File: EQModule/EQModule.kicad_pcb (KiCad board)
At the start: 2 copper layers, 30 x 38 mm, 13 parts, among them J1 SigIn, J2 SigOut, J3 TreblePot, J4 BassPot, J5 MidPot, J6 VolPot

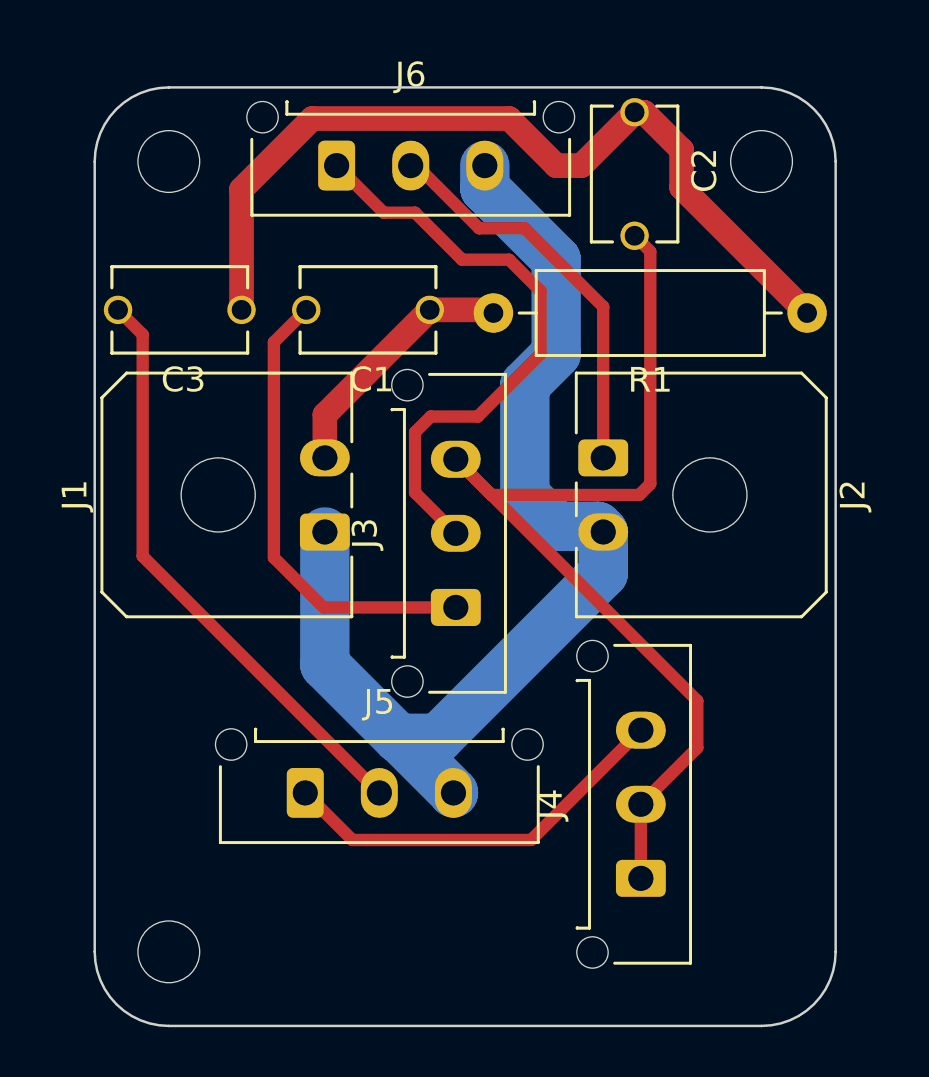
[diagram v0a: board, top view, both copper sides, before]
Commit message: Change connector footprints to contain 3D models. Make necessary PCB modifications to address errors found in the design
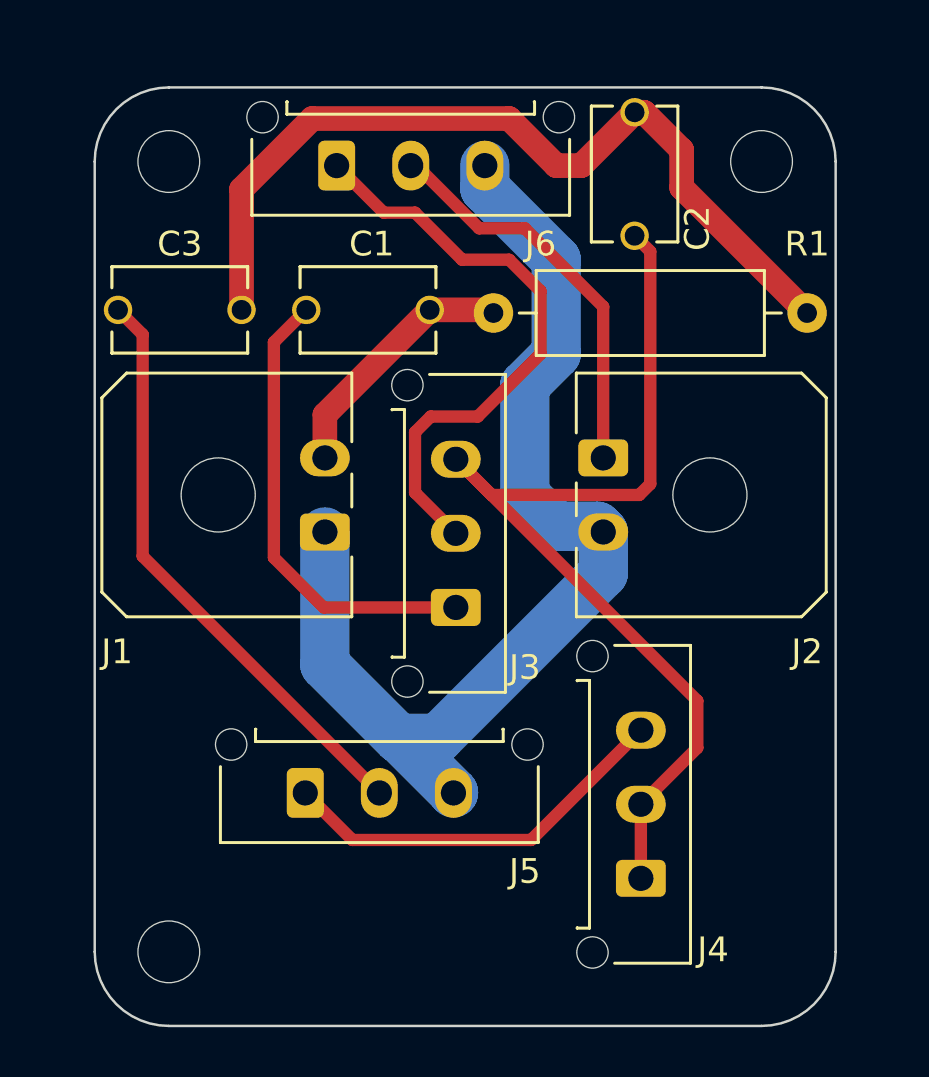
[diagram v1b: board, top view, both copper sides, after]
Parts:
- J1, J2: footprint Connector_Molex:Molex_Micro-Fit_3.0_43650-0200_1x02_P3.00mm_Horizontal -> CustomFootprints:Molex_Micro-Fit_3.0_43650-0200_1x02_P3.00mm_Horizontal
- J3, J4, J5, J6: footprint Connector_Molex:Molex_Micro-Fit_3.0_43650-0315_1x03_P3.00mm_Vertical -> CustomFootprints:Molex_Micro-Fit_3.0_43650-0315_1x03_P3.00mm_Vertical
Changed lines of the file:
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@@
   (net 8 "Net-(J3-Pin_2)")
   (net 9 "Net-(J4-Pin_3)")
-  (footprint "Connector_Molex:Molex_Micro-Fit_3.0_43650-0200_1x02_P3.00mm_Horizontal" (layer "F.Cu")
+  (footprint "CustomFootprints:Molex_Micro-Fit_3.0_43650-0200_1x02_P3.00mm_Horizontal" (layer "F.Cu")
     (at 148.59 62 -90)
     (descr "Molex Micro-Fit 3.0 Connector System, 43650-0200 (compatible alternatives: 43650-0201, 43650-0202), 2 Pins per row (https://www.molex.com/pdm_docs/sd/436500300_sd.pdf), generated with kicad-footprint-generator")
@@
     (property "ki_keywords" "screw terminal")
     (attr through_hole)
-    (fp_text reference "J2" (at 1.5 -10.12 90) (layer "F.SilkS")
-        (effects (font (size 1 1) (thickness 0.15)))
-    )
-    (fp_text value "SigOut" (at 1.5 -6.985 90) (layer "F.Fab")
-        (effects (font (size 1 1) (thickness 0.15)))
-    )
-    (fp_text user "${REFERENCE}" (at 1.5 -8.22 90) (layer "F.Fab")
+    (fp_text reference "J2" (at 7.85 -8.255) (layer "F.SilkS")
+        (effects (font (size 1 1) (thickness 0.15)))
+    )
+    (fp_text value "SigOut" (at 1.5 3.22 -90) (layer "F.Fab")
+        (effects (font (size 1 1) (thickness 0.15)))
+    )
+    (fp_text user "${REFERENCE}" (at 1.5 -8.22 -90) (layer "F.Fab")
         (effects (font (size 1 1) (thickness 0.15)))
     )
@@
       (rotate (xyz 0 0 0))
     )
+    (model "C:/Users/dillo/Downloads/436500200_stp/436500200.stp"
+      (offset (xyz 1.5 8.9 0.5))
+      (scale (xyz 1 1 1))
+      (rotate (xyz 0 0 180))
+    )
   )
   (footprint "Resistor_THT:R_Axial_DIN0309_L9.0mm_D3.2mm_P12.70mm_Horizontal" (layer "F.Cu")
@@
     (property "ki_keywords" "R res resistor")
     (attr through_hole)
-    (fp_text reference "R1" (at 6.35 -2.72) (layer "F.SilkS")
+    (fp_text reference "R1" (at 0 2.794) (layer "F.SilkS")
         (effects (font (size 1 1) (thickness 0.15)))
     )
@@
     )
   )
-  (footprint "Connector_Molex:Molex_Micro-Fit_3.0_43650-0315_1x03_P3.00mm_Vertical" (layer "F.Cu")
+  (footprint "CustomFootprints:Molex_Micro-Fit_3.0_43650-0315_1x03_P3.00mm_Vertical" (layer "F.Cu")
     (at 150.114 79.025 90)
     (descr "Molex Micro-Fit 3.0 Connector System, 43650-0315 (compatible alternatives: 43650-0316, 43650-0317), 3 Pins per row (http://www.molex.com/pdm_docs/sd/436500215_sd.pdf), generated with kicad-footprint-generator")
@@
     (property "ki_keywords" "screw terminal")
     (attr through_hole)
-    (fp_text reference "J4" (at 3 -3.67 90) (layer "F.SilkS")
-        (effects (font (size 1 1) (thickness 0.15)))
-    )
-    (fp_text value "BassPot" (at 3 -1.97 90) (layer "F.Fab")
+    (fp_text reference "J4" (at -2.89 2.921 180) (layer "F.SilkS")
+        (effects (font (size 1 1) (thickness 0.15)))
+    )
+    (fp_text value "BassPot" (at 3 4.5 90) (layer "F.Fab")
         (effects (font (size 1 1) (thickness 0.15)))
     )
@@
       (rotate (xyz 0 0 0))
     )
-  )
-  (footprint "Connector_Molex:Molex_Micro-Fit_3.0_43650-0315_1x03_P3.00mm_Vertical" (layer "F.Cu")
+    (model "C:/Users/dillo/Downloads/436500315_stp/436500315.stp"
+      (offset (xyz 3 1.9 10))
+      (scale (xyz 1 1 1))
+      (rotate (xyz 90 0 180))
+    )
+  )
+  (footprint "CustomFootprints:Molex_Micro-Fit_3.0_43650-0315_1x03_P3.00mm_Vertical" (layer "F.Cu")
     (at 137.795 50.165)
     (descr "Molex Micro-Fit 3.0 Connector System, 43650-0315 (compatible alternatives: 43650-0316, 43650-0317), 3 Pins per row (http://www.molex.com/pdm_docs/sd/436500215_sd.pdf), generated with kicad-footprint-generator")
@@
     (property "ki_keywords" "screw terminal")
     (attr through_hole)
-    (fp_text reference "J6" (at 3 -3.67) (layer "F.SilkS")
-        (effects (font (size 1 1) (thickness 0.15)))
-    )
-    (fp_text value "VolPot" (at 3 -1.97) (layer "F.Fab")
+    (fp_text reference "J6" (at 8.255 3.175) (layer "F.SilkS")
+        (effects (font (size 1 1) (thickness 0.15)))
+    )
+    (fp_text value "VolPot" (at 3 4.5) (layer "F.Fab")
         (effects (font (size 1 1) (thickness 0.15)))
     )
@@
       (rotate (xyz 0 0 0))
     )
-  )
-  (footprint "Connector_Molex:Molex_Micro-Fit_3.0_43650-0200_1x02_P3.00mm_Horizontal" (layer "F.Cu")
+    (model "C:/Users/dillo/Downloads/436500315_stp/436500315.stp"
+      (offset (xyz 3 1.9 10))
+      (scale (xyz 1 1 1))
+      (rotate (xyz 90 0 180))
+    )
+  )
+  (footprint "CustomFootprints:Molex_Micro-Fit_3.0_43650-0200_1x02_P3.00mm_Horizontal" (layer "F.Cu")
     (at 137.32 65 90)
     (descr "Molex Micro-Fit 3.0 Connector System, 43650-0200 (compatible alternatives: 43650-0201, 43650-0202), 2 Pins per row (https://www.molex.com/pdm_docs/sd/436500300_sd.pdf), generated with kicad-footprint-generator")
@@
     (property "ki_keywords" "screw terminal")
     (attr through_hole)
-    (fp_text reference "J1" (at 1.5 -10.12 90) (layer "F.SilkS")
-        (effects (font (size 1 1) (thickness 0.15)))
-    )
-    (fp_text value "SigIn" (at 1.5 -7.145 90) (layer "F.Fab")
+    (fp_text reference "J1" (at -4.85 -8.415 180) (layer "F.SilkS")
+        (effects (font (size 1 1) (thickness 0.15)))
+    )
+    (fp_text value "SigIn" (at 1.5 3.22 90) (layer "F.Fab")
         (effects (font (size 1 1) (thickness 0.15)))
     )
@@
       (rotate (xyz 0 0 0))
     )
+    (model "C:/Users/dillo/Downloads/436500200_stp/436500200.stp"
+      (offset (xyz 1.5 8.9 0.5))
+      (scale (xyz 1 1 1))
+      (rotate (xyz 0 0 180))
+    )
   )
   (footprint "MountingHole:MountingHole_2.5mm" (layer "F.Cu")
@@
     (pad "" np_thru_hole circle (at 0 0) (size 2.5 2.5) (drill 2.5) (layers "F&B.Cu" "*.Mask"))
   )
-  (footprint "Connector_Molex:Molex_Micro-Fit_3.0_43650-0315_1x03_P3.00mm_Vertical" (layer "F.Cu")
+  (footprint "CustomFootprints:Molex_Micro-Fit_3.0_43650-0315_1x03_P3.00mm_Vertical" (layer "F.Cu")
     (at 142.621 68.055 90)
     (descr "Molex Micro-Fit 3.0 Connector System, 43650-0315 (compatible alternatives: 43650-0316, 43650-0317), 3 Pins per row (http://www.molex.com/pdm_docs/sd/436500215_sd.pdf), generated with kicad-footprint-generator")
@@
     (property "ki_keywords" "screw terminal")
     (attr through_hole)
-    (fp_text reference "J3" (at 3 -3.67 90) (layer "F.SilkS")
-        (effects (font (size 1 1) (thickness 0.15)))
-    )
-    (fp_text value "TreblePot" (at 3 3.3 90) (layer "F.Fab")
+    (fp_text reference "J3" (at -2.43 2.794 180) (layer "F.SilkS")
+        (effects (font (size 1 1) (thickness 0.15)))
+    )
+    (fp_text value "TreblePot" (at 3 4.5 90) (layer "F.Fab")
         (effects (font (size 1 1) (thickness 0.15)))
     )
@@
       (rotate (xyz 0 0 0))
     )
+    (model "C:/Users/dillo/Downloads/436500315_stp/436500315.stp"
+      (offset (xyz 3 1.9 10))
+      (scale (xyz 1 1 1))
+      (rotate (xyz 90 0 180))
+    )
   )
   (footprint "CustomFootprints:FG26 Cap" (layer "F.Cu")
@@
     (property "ki_keywords" "cap capacitor")
     (attr through_hole)
-    (fp_text reference "C2" (at -0.15 -2.835 90) (layer "F.SilkS")
+    (fp_text reference "C2" (at 2.199 -2.54 -90) (layer "F.SilkS")
         (effects (font (size 1 1) (thickness 0.15)))
     )
@@
     )
   )
-  (footprint "Connector_Molex:Molex_Micro-Fit_3.0_43650-0315_1x03_P3.00mm_Vertical" (layer "F.Cu")
+  (footprint "CustomFootprints:Molex_Micro-Fit_3.0_43650-0315_1x03_P3.00mm_Vertical" (layer "F.Cu")
     (at 136.525 75.565)
     (descr "Molex Micro-Fit 3.0 Connector System, 43650-0315 (compatible alternatives: 43650-0316, 43650-0317), 3 Pins per row (http://www.molex.com/pdm_docs/sd/436500215_sd.pdf), generated with kicad-footprint-generator")
@@
     (property "ki_keywords" "screw terminal")
     (attr through_hole)
-    (fp_text reference "J5" (at 3 -3.67) (layer "F.SilkS")
-        (effects (font (size 1 1) (thickness 0.15)))
-    )
-    (fp_text value "MidPot" (at 3 -1.97) (layer "F.Fab")
+    (fp_text reference "J5" (at 8.89 3.175) (layer "F.SilkS")
+        (effects (font (size 1 1) (thickness 0.15)))
+    )
+    (fp_text value "MidPot" (at 3 4.5) (layer "F.Fab")
         (effects (font (size 1 1) (thickness 0.15)))
     )
@@
       (rotate (xyz 0 0 0))
     )
+    (model "C:/Users/dillo/Downloads/436500315_stp/436500315.stp"
+      (offset (xyz 3 1.9 10))
+      (scale (xyz 1 1 1))
+      (rotate (xyz 90 0 180))
+    )
   )
   (footprint "CustomFootprints:FG26 Cap" (layer "F.Cu")
@@
     (property "ki_keywords" "cap capacitor")
     (attr through_hole)
-    (fp_text reference "C3" (at -0.15 -2.835) (layer "F.SilkS")
+    (fp_text reference "C3" (at 0 2.667) (layer "F.SilkS")
         (effects (font (size 1 1) (thickness 0.15)))
     )
@@
     (property "ki_keywords" "cap capacitor")
     (attr through_hole)
-    (fp_text reference "C1" (at -0.15 -2.835) (layer "F.SilkS")
-        (effects (font (size 1 1) (thickness 0.15)))
-    )
+    (fp_text reference "C1" (at -0.15 2.667) (layer "F.SilkS")
+        (effects (font (size 1 1) (thickness 0.15)))
+    )
